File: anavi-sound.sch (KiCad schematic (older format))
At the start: 23 parts, among them U1 CAT24C32WI-GT3, U1 MAX98357

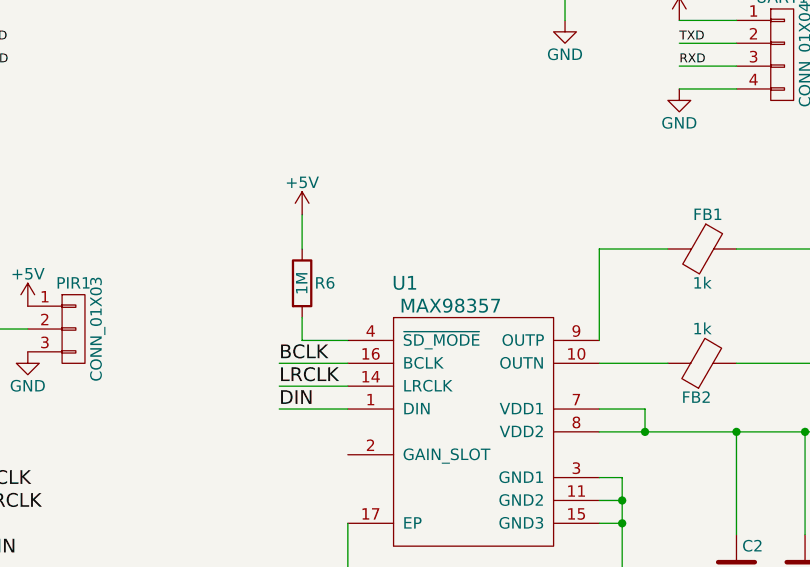
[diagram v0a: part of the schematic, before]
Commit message: anavi-sound.sch: Fix annotations
Signed-off-by: Leon Anavi <leon@anavi.org>
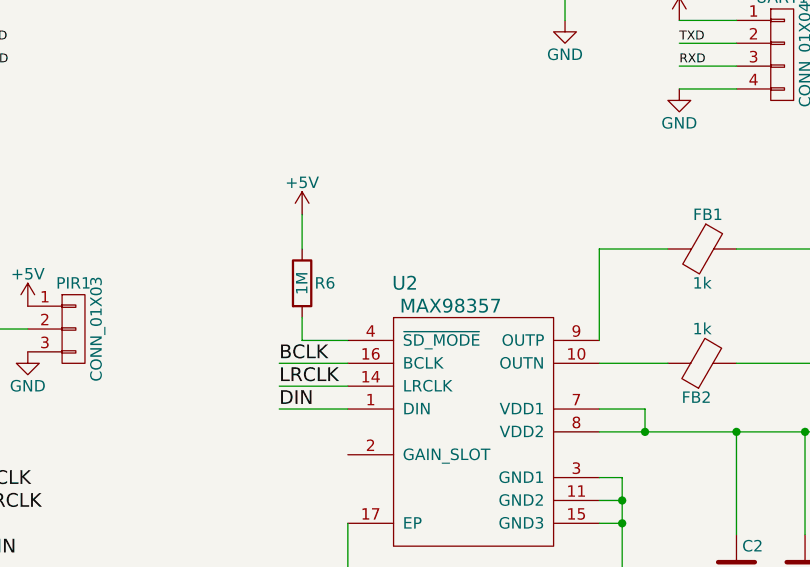
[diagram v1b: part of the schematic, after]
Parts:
- renumbered U1 to U2
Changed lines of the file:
@@
 NoConn ~ 5350 2800
 $Comp
-L MAX98357 U1
+L MAX98357 U2
 U 1 1 5AF4BF11
 P 7650 3900
-F 0 "U1" H 7350 4550 60  0000 C CNN
+F 0 "U2" H 7350 4550 60  0000 C CNN
 F 1 "MAX98357" H 7550 4450 60  0000 C CNN
 F 2 "QFN:qfn16_1ep_3x3_p05" H 7650 3900 60  0001 C CNN

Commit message: anavi-sound.sch: Add terminal for the speaker
Signed-off-by: Leon Anavi <leon@anavi.org>
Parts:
- SP1: footprint (none) -> Terminal_Blocks:TerminalBlock_Pheonix_MKDS1.5-2pol
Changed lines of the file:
@@
 F 0 "SP1" H 10200 3750 50  0000 C TNN
 F 1 "Screw_Terminal_1x02" V 10050 3500 50  0000 C TNN
-F 2 "" H 10200 3275 50  0001 C CNN
+F 2 "Terminal_Blocks:TerminalBlock_Pheonix_MKDS1.5-2pol" H 10200 3275 50  0001 C CNN
 F 3 "" H 10175 3500 50  0001 C CNN
 	1    10200 3500
@@
 $EndComp
 $Comp
-L GND #PWR?
+L GND #PWR015
 U 1 1 5AF4D492
 P 9500 4650
-F 0 "#PWR?" H 9500 4400 50  0001 C CNN
+F 0 "#PWR015" H 9500 4400 50  0001 C CNN
 F 1 "GND" H 9500 4500 50  0000 C CNN
 F 2 "" H 9500 4650 50  0001 C CNN
@@
 $EndComp
 $Comp
-L GND #PWR?
+L GND #PWR016
 U 1 1 5AF4D53E
 P 9800 4650
-F 0 "#PWR?" H 9800 4400 50  0001 C CNN
+F 0 "#PWR016" H 9800 4400 50  0001 C CNN
 F 1 "GND" H 9800 4500 50  0000 C CNN
 F 2 "" H 9800 4650 50  0001 C CNN
@@
 $EndComp
 $Comp
-L GND #PWR?
+L GND #PWR017
 U 1 1 5AF4DEBE
 P 8300 4650
-F 0 "#PWR?" H 8300 4400 50  0001 C CNN
+F 0 "#PWR017" H 8300 4400 50  0001 C CNN
 F 1 "GND" H 8300 4500 50  0000 C CNN
 F 2 "" H 8300 4650 50  0001 C CNN
@@
 $EndComp
 $Comp
-L GND #PWR?
+L GND #PWR018
 U 1 1 5AF4E13A
 P 7100 4650
-F 0 "#PWR?" H 7100 4400 50  0001 C CNN
+F 0 "#PWR018" H 7100 4400 50  0001 C CNN
 F 1 "GND" H 7100 4500 50  0000 C CNN
 F 2 "" H 7100 4650 50  0001 C CNN
@@
 $EndComp
 $Comp
-L +5V #PWR?
+L +5V #PWR019
 U 1 1 5AF4E41B
 P 6900 2950
-F 0 "#PWR?" H 6900 2800 50  0001 C CNN
+F 0 "#PWR019" H 6900 2800 50  0001 C CNN
 F 1 "+5V" H 6900 3090 50  0000 C CNN
 F 2 "" H 6900 2950 50  0001 C CNN
@@
 $EndComp
 $Comp
-L GND #PWR?
+L GND #PWR020
 U 1 1 5AF4ECEB
 P 8800 4650
-F 0 "#PWR?" H 8800 4400 50  0001 C CNN
+F 0 "#PWR020" H 8800 4400 50  0001 C CNN
 F 1 "GND" H 8800 4500 50  0000 C CNN
 F 2 "" H 8800 4650 50  0001 C CNN
@@
 $EndComp
 $Comp
-L GND #PWR?
+L GND #PWR021
 U 1 1 5AF4ED2B
 P 9100 4650
-F 0 "#PWR?" H 9100 4400 50  0001 C CNN
+F 0 "#PWR021" H 9100 4400 50  0001 C CNN
 F 1 "GND" H 9100 4500 50  0000 C CNN
 F 2 "" H 9100 4650 50  0001 C CNN
@@
 $EndComp
 $Comp
-L +5V #PWR?
+L +5V #PWR022
 U 1 1 5AF4EF16
 P 9250 3900
-F 0 "#PWR?" H 9250 3750 50  0001 C CNN
+F 0 "#PWR022" H 9250 3750 50  0001 C CNN
 F 1 "+5V" H 9250 4040 50  0000 C CNN
 F 2 "" H 9250 3900 50  0001 C CNN

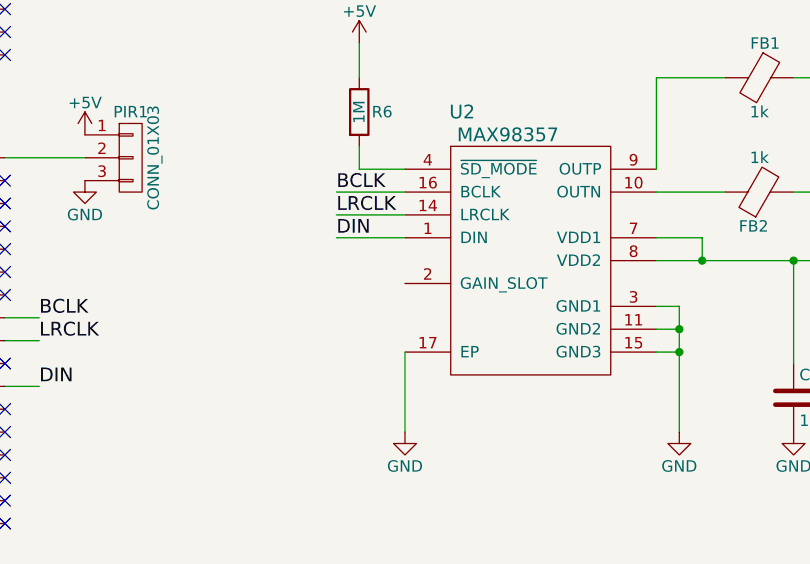
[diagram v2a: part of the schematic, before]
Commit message: MAX98357A routing
Update footprint and routing.

Signed-off-by: Leon Anavi <leon@anavi.org>
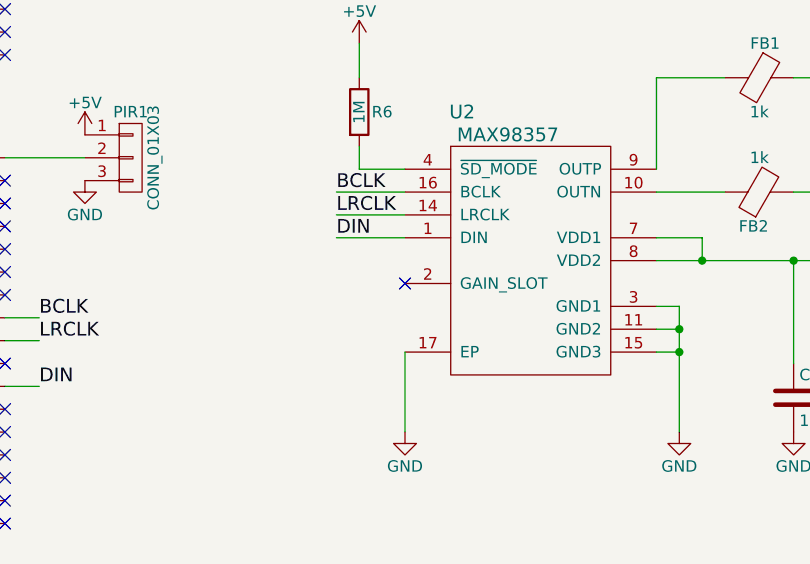
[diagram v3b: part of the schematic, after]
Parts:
- U2: footprint QFN:qfn16_1ep_3x3_p05 -> Housings_DFN_QFN:QFN-16-1EP_3x3mm_Pitch0.5mm
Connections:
- no-connect marks 18 -> 19
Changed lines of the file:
@@
 F 0 "U2" H 7350 4550 60  0000 C CNN
 F 1 "MAX98357" H 7550 4450 60  0000 C CNN
-F 2 "QFN:qfn16_1ep_3x3_p05" H 7650 3900 60  0001 C CNN
+F 2 "Housings_DFN_QFN:QFN-16-1EP_3x3mm_Pitch0.5mm" H 7650 3900 60  0001 C CNN
 F 3 "" H 7650 3900 60  0001 C CNN
 	1    7650 3900
@@
 Text Label 5500 4250 0    60   ~ 0
 LRCLK
+NoConn ~ 7100 4000
 $EndSCHEMATC
